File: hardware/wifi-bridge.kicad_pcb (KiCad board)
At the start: 4 copper layers, 50 x 35 mm, 84 parts, among them J201 USB-MINI-B-SMD, P101 CONN_1, P102 CONN_1, P103 CONN_1, P104 CON-SENSOR, Q101 MOS_P, SW101 ERASE, SW102 RESET, U101 AT91SAM3SXB, U102 ESP8266_WROOM02, U103 M24C64, U104 DRILL, U105 DRILL, U106 DRILL, U107 DRILL, U201 82400152, U202 AAT3681A, U203 PAM2301, U204 FAN4860, X101 16MHz

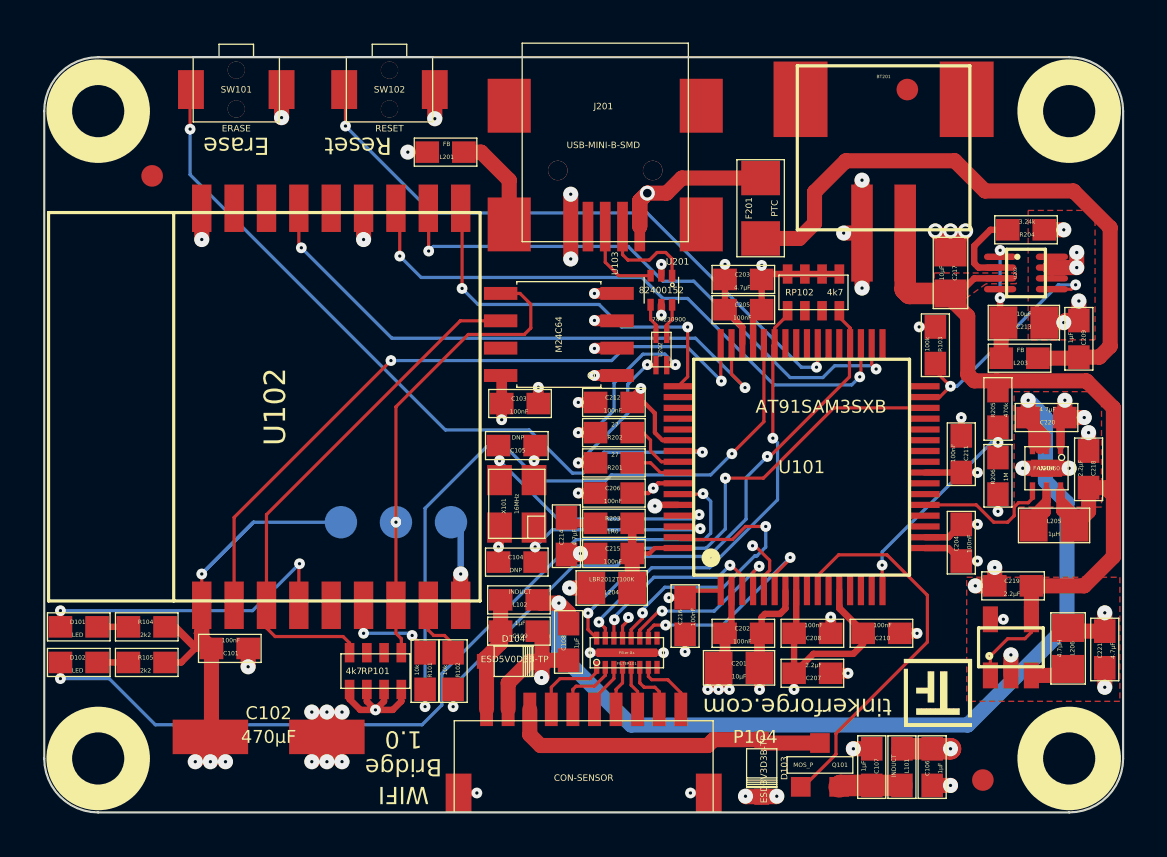
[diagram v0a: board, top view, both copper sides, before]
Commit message: add hints to the schematic, add demo code
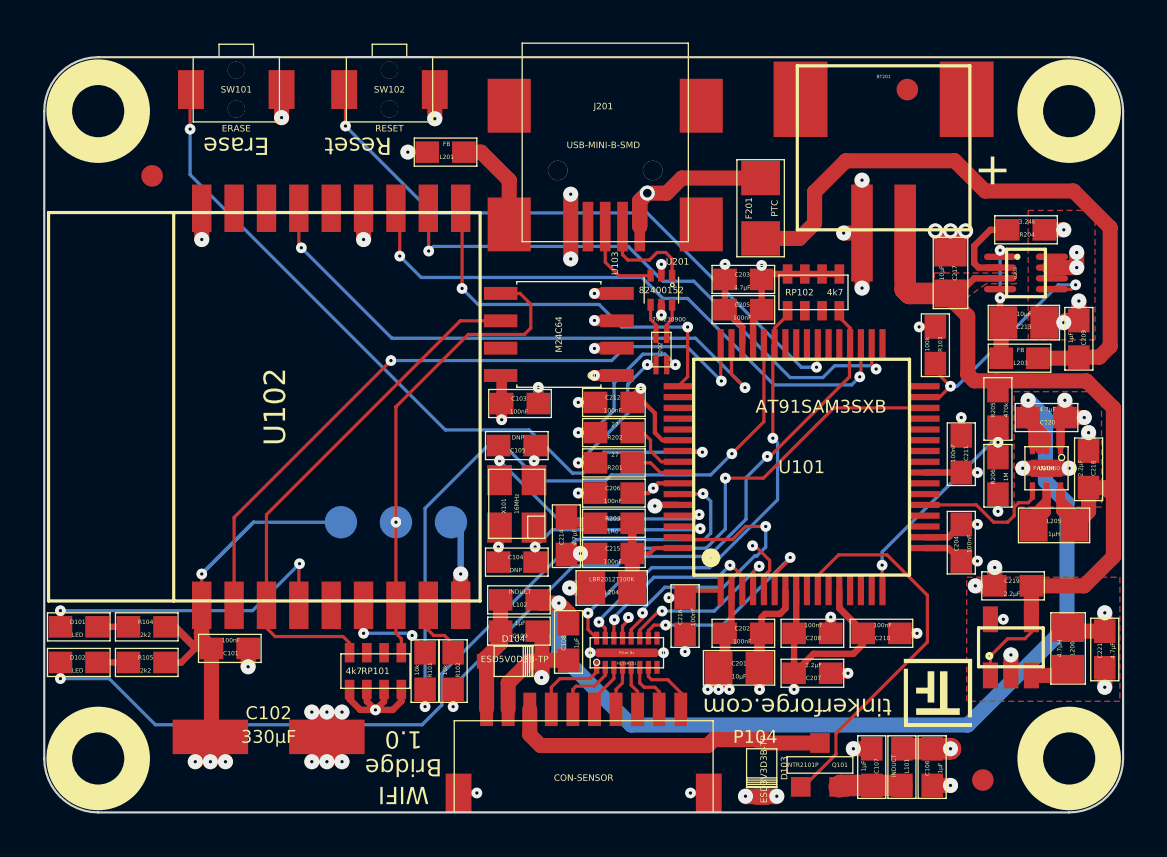
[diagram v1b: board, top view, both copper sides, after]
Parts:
- C102: value 470µF -> 330µF
- Q101: value MOS_P -> NTR2101P
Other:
- board text added: "+"

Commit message: fix pcb (erase button to vcc)
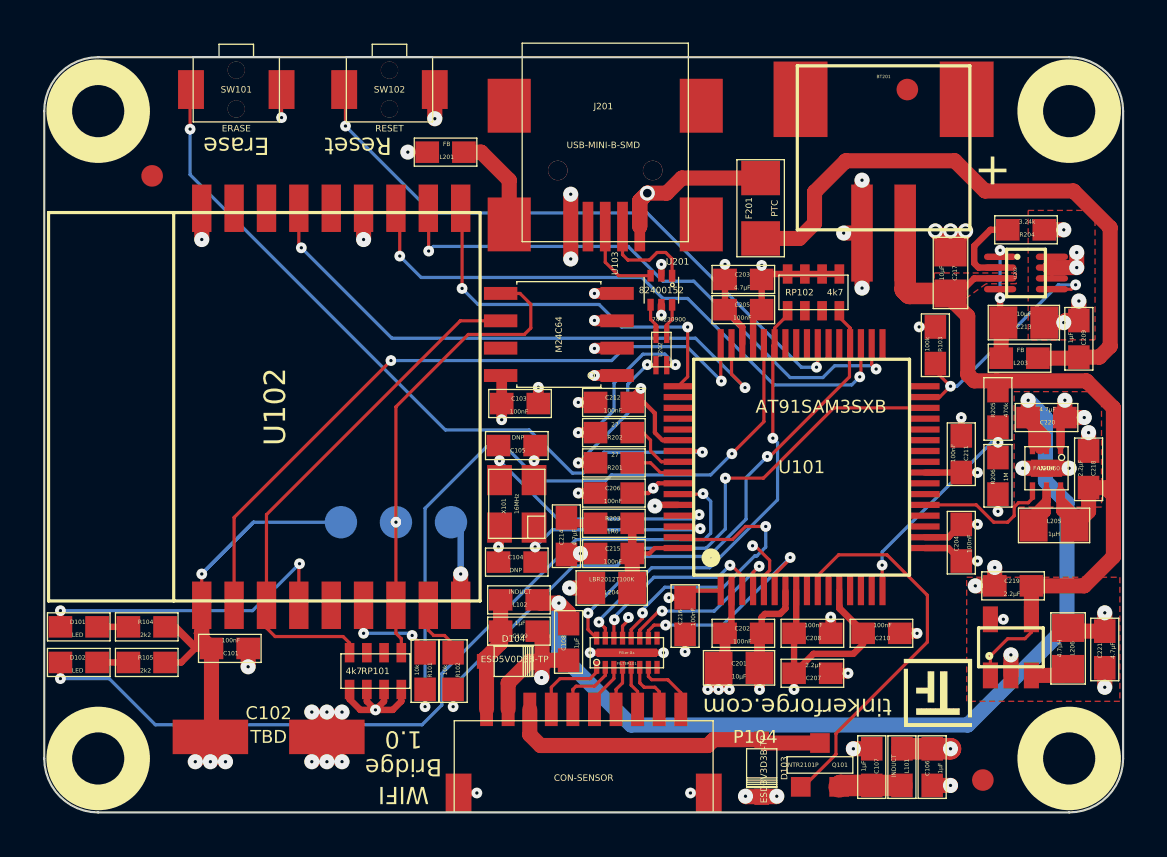
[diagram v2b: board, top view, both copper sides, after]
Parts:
- C102: value 330µF -> TBD
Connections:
- SW101 pad 2: GND -> 3V3
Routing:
- net 3V3: track 210.4 -> 225.8 mm, vias 16 -> 17
- net GND: track 282.9 -> 275.1 mm, vias 66 -> 65
